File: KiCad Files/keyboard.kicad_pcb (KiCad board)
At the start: 2 copper layers, 333.4 x 100 mm, 208 parts, among them J1 Conn_01x10, J2 Button, J3 78171-0004, J5 Conn_01x03_Male, U1 SOT-23-5 5.5V 3.3V 500mA, U2 RP2040, U3 TXS0101DCK, Y1 3225_4P 12MHz

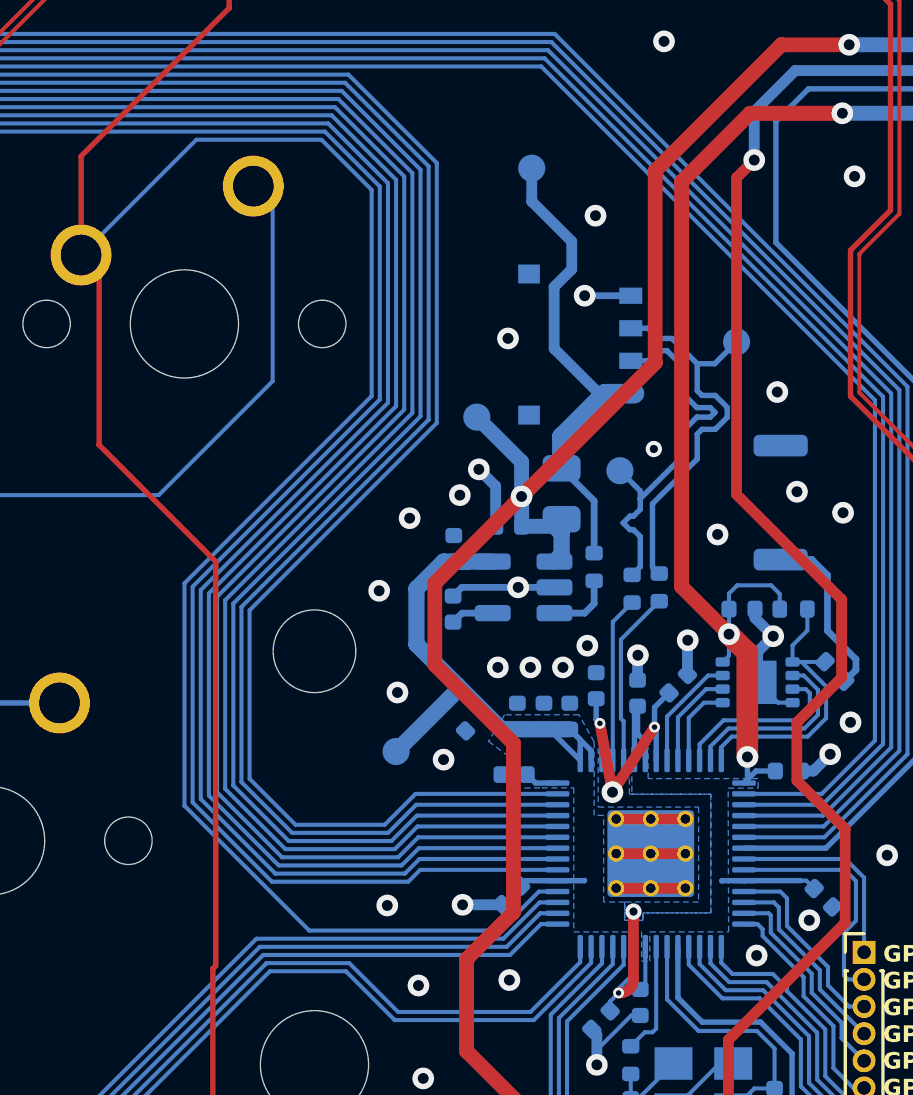
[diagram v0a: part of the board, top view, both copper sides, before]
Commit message: rotated udb-s connector as requested and generated updated production files
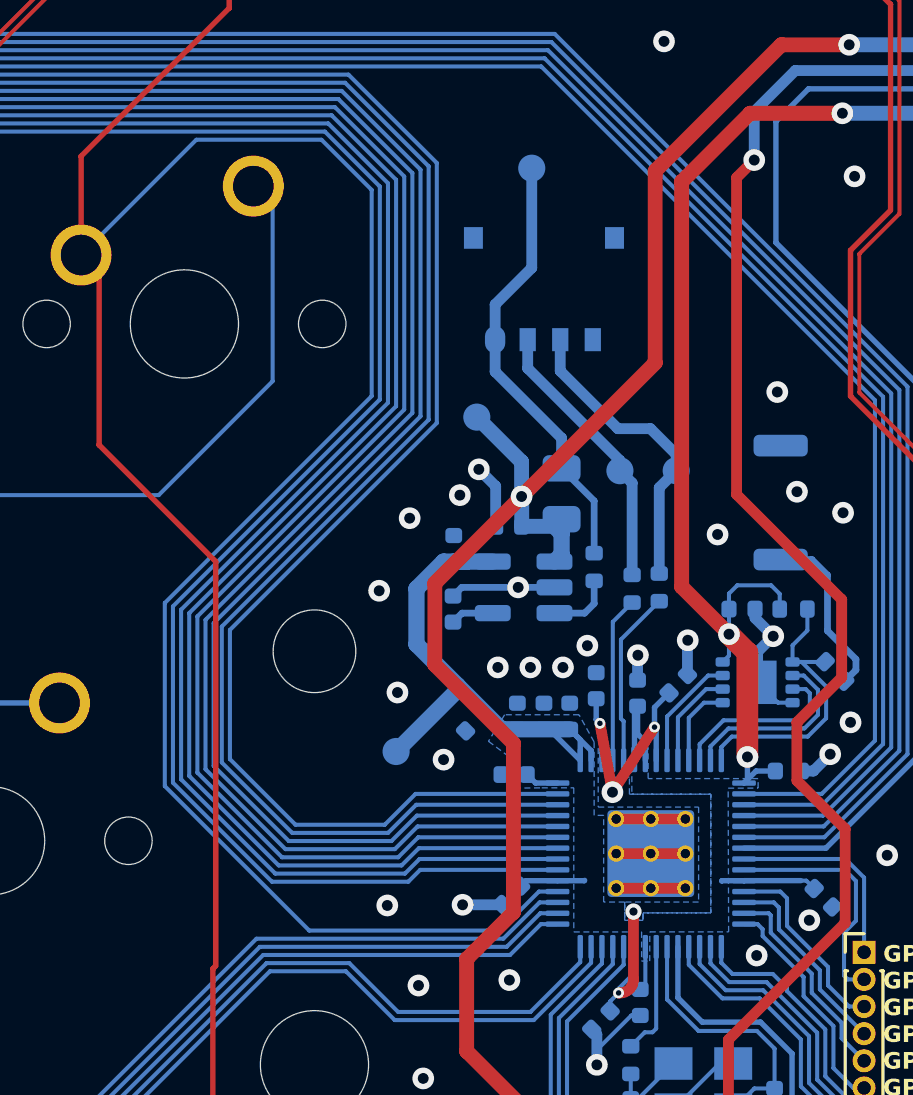
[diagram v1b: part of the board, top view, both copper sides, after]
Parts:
- moved TP6 5.25 mm to (287.6, 50.8)
- moved J3 3.21 mm to (282.7, 45.9), turned to 0 degrees
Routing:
- net D-: track 14.3 -> 10.3 mm
- net D+: track 14.8 -> 11.4 mm
- net VBUS: track 19.0 -> 16.3 mm
- net GND: track 57.6 -> 55.9 mm, vias 51 -> 47
- net col6: track 280.3 -> 280.9 mm
- net col5: track 280.1 -> 280.7 mm
- net col12: track 189.1 -> 189.7 mm
- net col11: track 180.8 -> 181.4 mm
- net col10: track 210.1 -> 210.7 mm
- net col7: track 241.6 -> 242.2 mm
- net col8: track 245.1 -> 245.7 mm
- net col9: track 203.2 -> 203.8 mm
- net col13: track 143.1 -> 143.7 mm
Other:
- board text added: "USB D+"
- board text removed: "USB +D"
